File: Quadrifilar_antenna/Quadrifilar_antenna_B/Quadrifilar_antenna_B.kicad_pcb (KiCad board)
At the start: 2 copper layers, 95 x 100 mm, 17 parts, among them J1 SMA

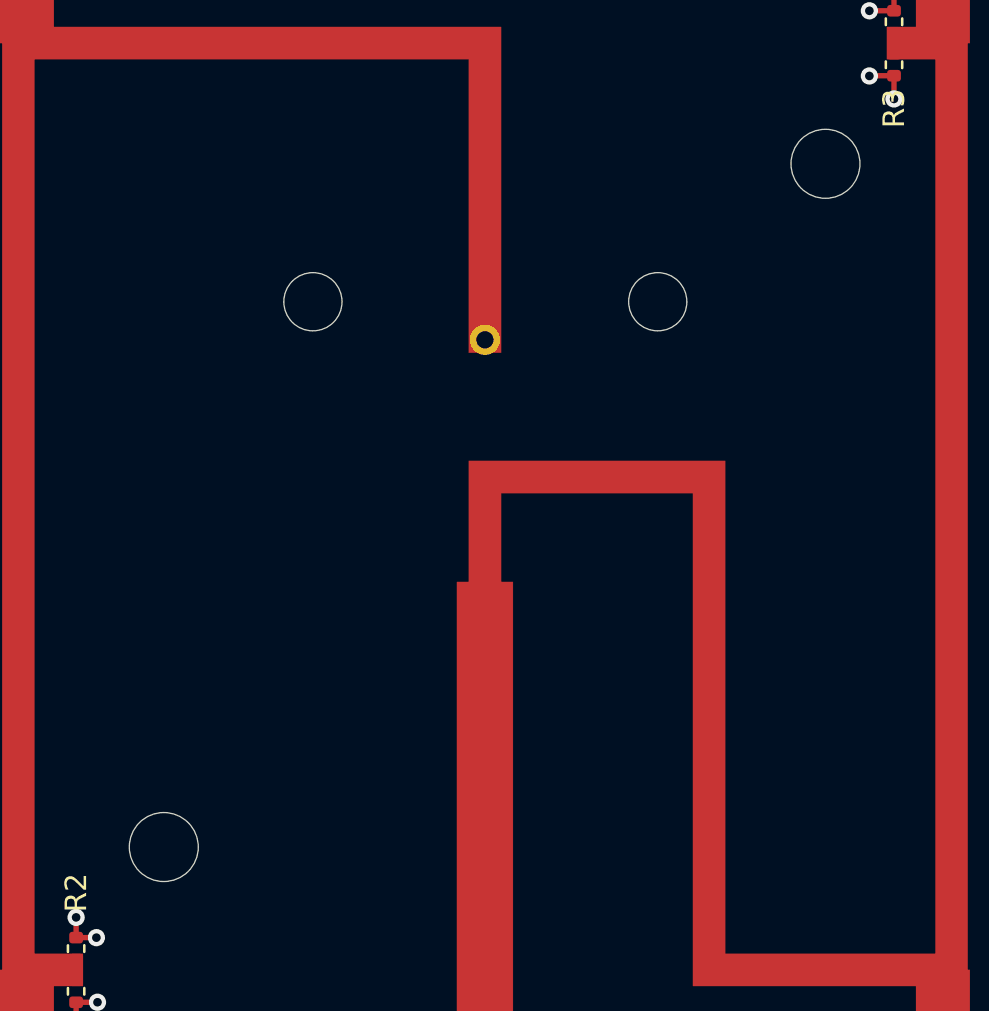
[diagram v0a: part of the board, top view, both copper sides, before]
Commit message: - added quadrifilar part C and mech assembly
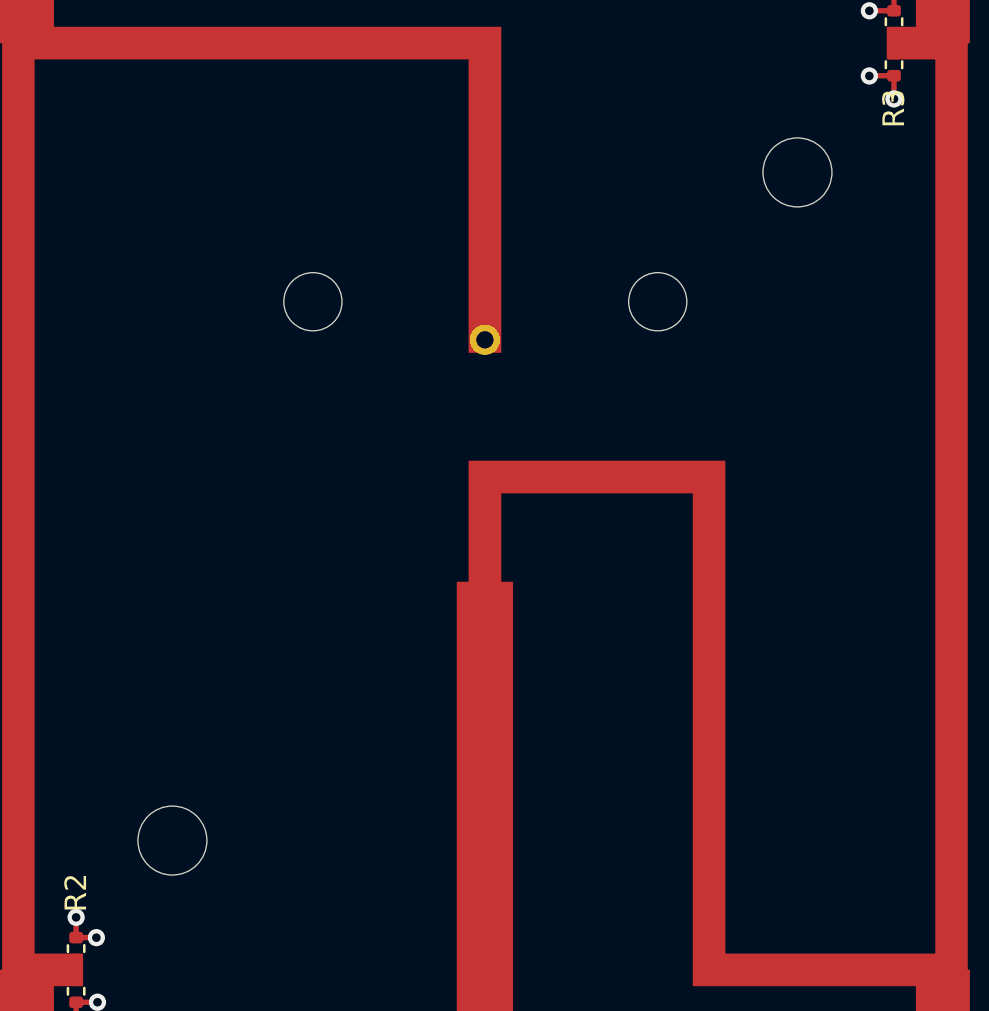
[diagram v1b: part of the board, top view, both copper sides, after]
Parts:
- moved   1.36 mm to (160.7, 59.4)
- moved   0.50 mm to (131.7, 90.4)
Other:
- board text added: "Copyright (C) 2021 Ricardo Goncalves"
- board text removed: "Copyright (C) Ricardo Goncalves"
